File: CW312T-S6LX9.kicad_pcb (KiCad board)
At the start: 2 copper layers, 58.7 x 53.7 mm, 41 parts, among them P1 PCIEx4 EDGE CONNECTOR, U1 XC6SLX9-3TQG144, U2 SST25VF040B-50-4C-SAF-T

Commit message: updated cw312t template
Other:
- outline, holes or cut-outs redrawn

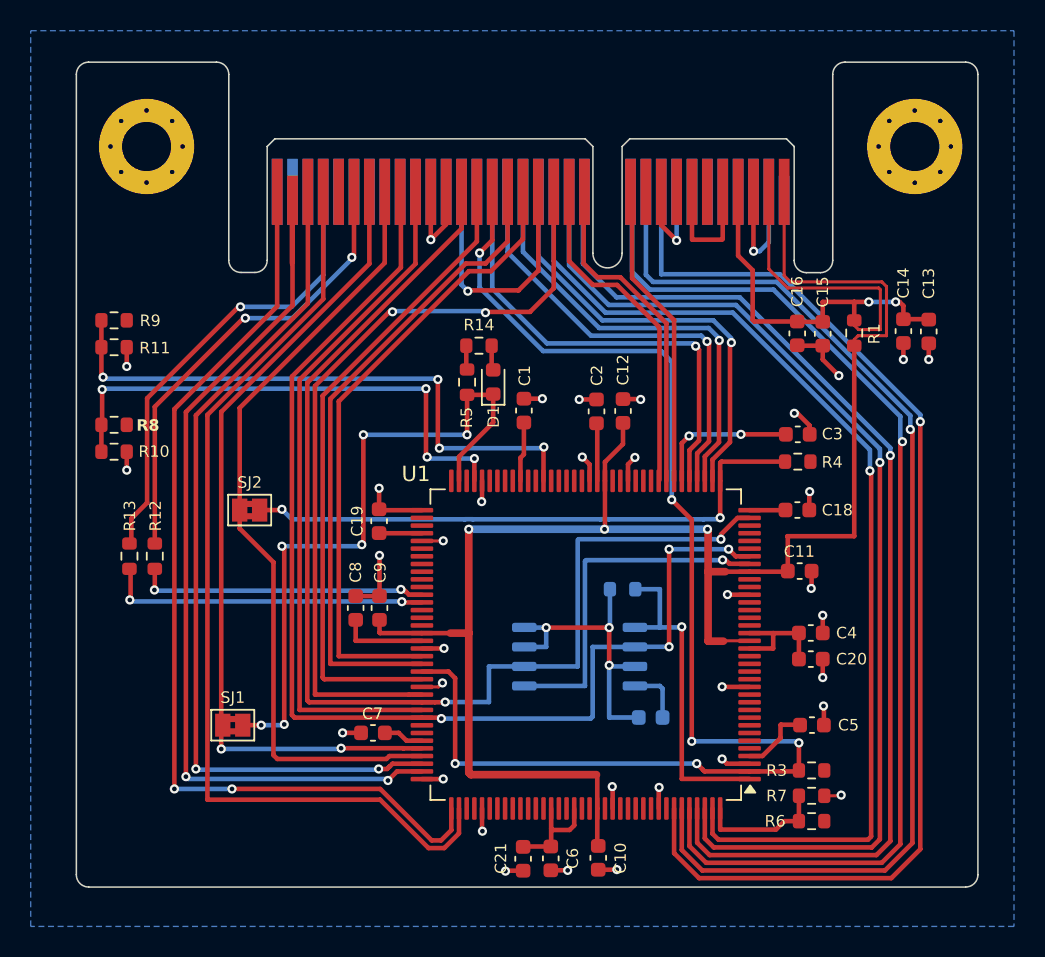
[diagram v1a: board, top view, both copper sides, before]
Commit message: added inner layers for gnd and pwr planes, added silkscreen, updated cw312t template
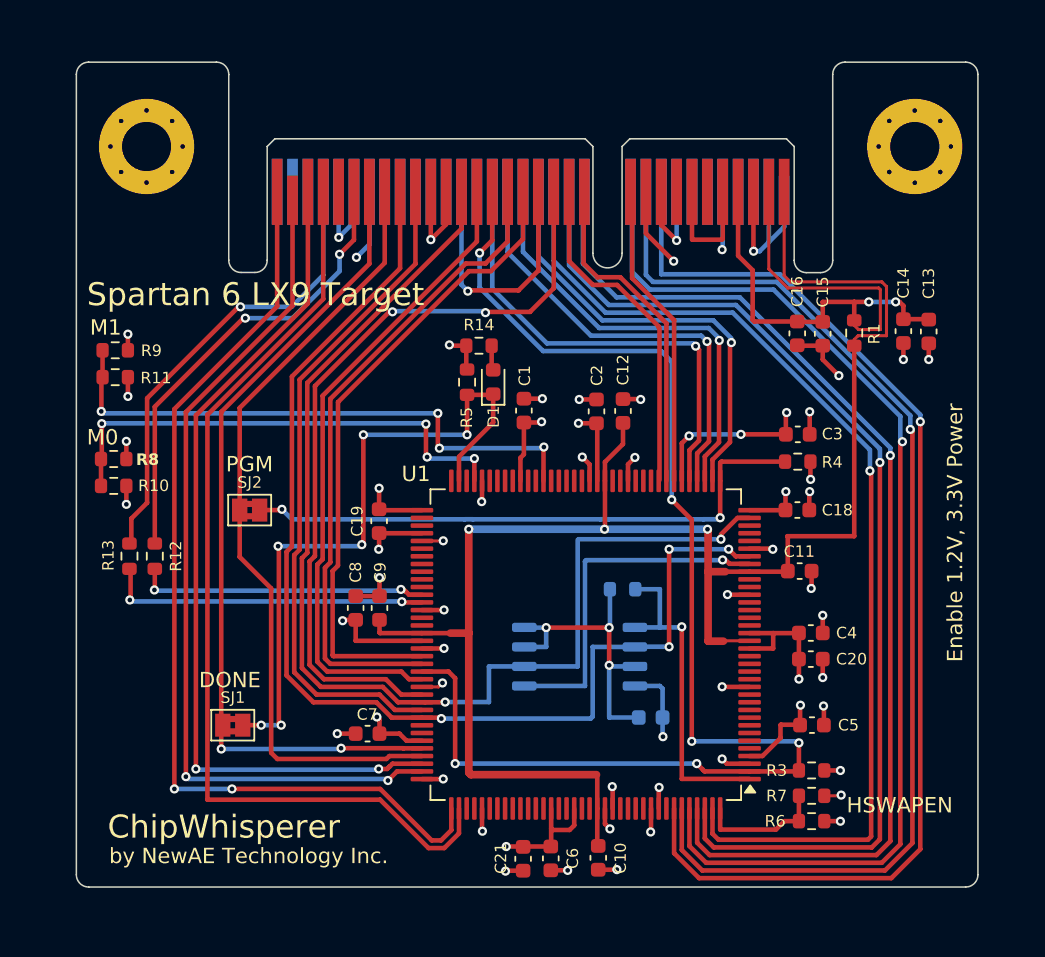
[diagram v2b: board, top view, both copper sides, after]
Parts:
- added PCB1: CE Symbol, Silkscrren_Symbols:CE-Logo_8.5x6mm_SilkScreen, F.Cu at (101.7, 100.5)
- added PCB2: Pb_Free Symbol, Silkscrren_Symbols:Pb_Free_8.0x8.0mm_SilkScreen, F.Cu at (100.6, 91.2)
- added PCB3: UKCA symbol, Silkscrren_Symbols:UKCA-Logo_8x8mm_SilkScreen, F.Cu at (91.7, 91.3)
- added PCB4: WEEE SYMBOL, Silkscrren_Symbols:WEEE-Logo_5.6x8mm_SilkScreen, F.Cu at (91.2, 99.6)
- moved R10 2.23 mm to (89.2, 79.3)
- moved R8 2.23 mm to (89.2, 77.5)
- moved R11 1.95 mm to (89.2, 72.2)
- moved R9 1.95 mm to (89.2, 70.5)
- moved C7 0.35 mm to (105.7, 95.4)
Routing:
- net VCC: track 71.8 -> 110.3 mm, vias 5 -> 28
- net GND: track 96.5 -> 105.4 mm, vias 38 -> 40
- net /XC6SLX9-3TQG144_2/TMS: track 60.2 -> 56.2 mm
- net /XC6SLX9-3TQG144_1/M0: track 34.1 -> 32.0 mm
- net /XC6SLX9-3TQG144_1/M1: track 39.4 -> 37.4 mm
- net /XC6SLX9-3TQG144_1/MOSI: track 78.0 -> 77.0 mm
- net /CW312T-Connector/MISO: track 44.8 -> 43.9 mm
- net /XC6SLX9-3TQG144_1/SCK: track 77.4 -> 76.7 mm
- net /CW312T-Connector/nRST: track 51.6 -> 50.9 mm
- net /CW312T-Connector/GPIO1: track 42.3 -> 42.9 mm
- added copper zone on In2.Cu, net GND
- added copper zone on In1.Cu, net VCC
- removed copper zone on B.Cu, net GND
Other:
- copper layers 2 -> 4
- board text added: "0 1"
- board text added: "1 1"
- board text added: "ChipWhisperer"
- board text added: "DONE"
- board text added: "Enable 1.2V, 3.3V Power"
- board text added: "FPGA Config."
- board text added: "HSWAPEN"
- board text added: "M0"
- board text added: "M1"
- board text added: "Mode"
- board text added: "NewAE Technology Inc. NAE-CW312T-S6LX9 RoHs / Pb-Free"
- board text added: "PGM"
- board text added: "SPI Flash CW-SPI"
- board text added: "SPI Flash Parts"
- board text added: "Spartan 6 LX9 Target"
- board text added: "by NewAE Technology Inc."

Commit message: first draft - ready for review
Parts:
- moved C5 0.91 mm to (134.7, 95.8)
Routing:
- net VCC: track 110.3 -> 109.1 mm
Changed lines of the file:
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@@
 	(footprint "Capacitor_SMD:C_0603_1608Metric"
 		(layer "F.Cu")
-		(at 134.6 94.846318)
+		(at 134.65 95.75)
 		(descr "Capacitor SMD 0603 (1608 Metric), square (rectangular) end terminal, IPC_7351 nominal, (Body size source: IPC-SM-782 page 76, https://www.pcb-3d.com/wordpress/wp-content/uploads/ipc-sm-782a_amendment_1_and_2.pdf), generated with kicad-footprint-generator")
 		(tags "capacitor")
@@
 	)
 	(segment
+		(start 133.875 95.75)
+		(end 133 95.75)
+		(width 0.3)
+		(layer "F.Cu")
+		(net 1)
+	)
+	(segment
 		(start 107.75 95.4)
 		(end 106.45 95.4)
@@
 	)
 	(segment
+		(start 133 95.75)
+		(end 131.891182 96.858818)
+		(width 0.3)
+		(layer "F.Cu")
+		(net 1)
+	)
+	(segment
 		(start 126.6 76.026038)
 		(end 126.125 76.501038)
@@
 	)
 	(segment
+		(start 133.875 94.65)
+		(end 133.875 95.75)
+		(width 0.3)
+		(layer "F.Cu")
+		(net 1)
+	)
+	(segment
 		(start 130.537501 88.858818)
 		(end 132.075 88.858818)
@@
 	)
 	(segment
-		(start 133.825 94.846318)
-		(end 133.825 93.575)
-		(width 0.3)
-		(layer "F.Cu")
-		(net 1)
-	)
-	(segment
 		(start 136.446318 101.096318)
 		(end 136.45 101.1)
@@
 	)
 	(segment
-		(start 133.775 94.771318)
-		(end 133.7 94.846318)
-		(width 0.3)
-		(layer "F.Cu")
-		(net 1)
-	)
-	(segment
 		(start 134.5 78.840997)
 		(end 134.511357 78.852354)
@@
 	)
 	(segment
-		(start 132.55 94.821318)
-		(end 132.55 95.686939)
-		(width 0.3)
-		(layer "F.Cu")
-		(net 1)
-	)
-	(segment
-		(start 133.8 94.821318)
-		(end 132.6 94.821318)
-		(width 0.3)
-		(layer "F.Cu")
-		(net 1)
-	)
-	(segment
 		(start 110.641182 87.358818)
 		(end 110.65 87.35)
@@
 	)
 	(segment
-		(start 131.378121 96.858818)
-		(end 130.537501 96.858818)
-		(width 0.3)
-		(layer "F.Cu")
-		(net 1)
-	)
-	(segment
 		(start 115.625001 78.946318)
 		(end 115.625001 77.45)
@@
 	)
 	(segment
+		(start 131.891182 96.858818)
+		(end 130.537501 96.858818)
+		(width 0.3)
+		(layer "F.Cu")
+		(net 1)
+	)
+	(segment
 		(start 111.049997 70.149997)
 		(end 111 70.1)
@@
 	)
 	(segment
-		(start 133.825 94.846318)
-		(end 133.8 94.821318)
-		(width 0.3)
-		(layer "F.Cu")
-		(net 1)
-	)
-	(segment
 		(start 126.137501 78.933817)
 		(end 126.125 78.946318)
@@
 	)
 	(segment
-		(start 132.55 95.686939)
-		(end 131.378121 96.858818)
-		(width 0.3)
-		(layer "F.Cu")
-		(net 1)
-	)
-	(segment
 		(start 115.625001 77.45)
 		(end 115.85 77.225001)
@@
 	)
 	(segment
-		(start 133.825 93.575)
-		(end 133.85 93.55)
-		(width 0.3)
-		(layer "F.Cu")
-		(net 1)
-	)
-	(segment
 		(start 130.537501 80.858818)
 		(end 132.8625 80.858818)
@@
 	)
 	(segment
-		(start 132.6 94.821318)
-		(end 132.575 94.846318)
-		(width 0.3)
-		(layer "F.Cu")
-		(net 1)
-	)
-	(segment
 		(start 133.675 90.475)
 		(end 133.75 90.55)
@@
 	)
 	(via
-		(at 133.85 93.55)
+		(at 133.875 94.65)
 		(size 0.6)
 		(drill 0.3)
@@
 	)
 	(segment
+		(start 135.4 95.725)
+		(end 135.425 95.75)
+		(width 0.3)
+		(layer "F.Cu")
+		(net 2)
+	)
+	(segment
 		(start 140.550003 71.049997)
 		(end 140.55 71.05)
@@
 	)
 	(segment
-		(start 135.3 70.15)
-		(end 133.665005 70.15)
+		(start 128.255202 97.358818)
+		(end 130.537502 97.358818)
 		(width 0.3)
 		(layer "F.Cu")
@@
 	)
 	(segment
-		(start 135.375 93.625)
-		(end 135.35 93.6)
-		(width 0.2)
+		(start 135.3 70.15)
+		(end 133.665005 70.15)
+		(width 0.3)
 		(layer "F.Cu")
 		(net 2)
@@
 	)
 	(segment
-		(start 135.375 94.846318)
-		(end 135.375 93.625)
-		(width 0.3)
-		(layer "F.Cu")
-		(net 2)
-	)
-	(segment
 		(start 106.45 86.446318)
 		(end 106.45 85.25)
@@
 	)
 	(segment
-		(start 130.537502 97.358818)
-		(end 129.058818 97.358818)
-		(width 0.3)
-		(layer "F.Cu")
-		(net 2)
-	)
-	(segment
 		(start 115.8 104.321318)
 		(end 114.678682 104.321318)
@@
 	)
 	(segment
+		(start 128.105202 97.208818)
+		(end 128.255202 97.358818)
+		(width 0.3)
+		(layer "F.Cu")
+		(net 2)
+	)
+	(segment
 		(start 120.125001 78.946318)
 		(end 120.125001 77.875001)
@@
 	)
 	(segment
+		(start 135.4 94.6)
+		(end 135.4 95.725)
+		(width 0.3)
+		(layer "F.Cu")
+		(net 2)
+	)
+	(segment
 		(start 140.550003 69.975001)
 		(end 140.550003 71.049997)
@@
 	)
 	(segment
-		(start 129.058818 97.358818)
-		(end 128.75 97.05)
-		(width 0.3)
-		(layer "F.Cu")
-		(net 2)
-	)
-	(segment
 		(start 120.125001 77.875001)
 		(end 119.65 77.4)
@@
 	)
 	(via
-		(at 128.75 97.05)
+		(at 128.105202 97.208818)
 		(size 0.6)
 		(drill 0.3)
@@
 	)
 	(via
-		(at 135.35 93.6)
+		(at 135.4 94.6)
 		(size 0.6)
 		(drill 0.3)
@@
 	)
 	(segment
-		(start 133.75 96)
-		(end 133.75 97.796318)
+		(start 126.775 81.482795)
+		(end 125.470846 80.178641)
 		(width 0.3)
 		(layer "F.Cu")
@@
 	)
 	(segment
-		(start 126.775 95.9)
+		(start 126.775 96.65)
 		(end 126.775 81.482795)
 		(width 0.3)
@@
 	)
 	(segment
-		(start 113.79 63.288958)
-		(end 113.79 60.135)
+		(start 133.75 96.85)
+		(end 133.75 97.796318)
 		(width 0.3)
 		(layer "F.Cu")
@@
 	)
 	(segment
-		(start 126.775 81.482795)
-		(end 125.470846 80.178641)
+		(start 113.79 63.288958)
+		(end 113.79 60.135)
 		(width 0.3)
 		(layer "F.Cu")
@@
 	)
 	(via
-		(at 126.775 95.9)
+		(at 126.775 96.65)
 		(size 0.6)
 		(drill 0.3)
@@
 	)
 	(via
-		(at 133.75 96)
+		(at 133.75 96.85)
 		(size 0.6)
 		(drill 0.3)
@@
 	)
 	(segment
-		(start 133.75 96)
-		(end 133.65 95.9)
+		(start 126.866182 96.558818)
+		(end 133.458818 96.558818)
+		(width 0.3)
+		(layer "B.Cu")
+		(net 31)
+	)
+	(segment
+		(start 126.775 96.65)
+		(end 126.866182 96.558818)
 		(width 0.3)
 		(layer "B.Cu")
@@
 	)
 	(segment
-		(start 112.964479 64.114479)
-		(end 112.964479 66.364479)
+		(start 133.458818 96.558818)
+		(end 133.75 96.85)
 		(width 0.3)
 		(layer "B.Cu")
@@
 	)
 	(segment
-		(start 133.65 95.9)
-		(end 126.775 95.9)
+		(start 112.964479 64.114479)
+		(end 112.964479 66.364479)
 		(width 0.3)
 		(layer "B.Cu")
@@
 		(polygon
 			(pts
-				(xy 79.5 49.4) (xy 150.1 49.4) (xy 150.2 49.5) (xy 150.2 108.25) (xy 79.5 108.25) (xy 79.5 49.4)
+				(xy 79.5 49.4) (xy 150.1 49.4) (xy 150.2 49.5) (xy 150.2 108.25) (xy 79.5 108.25)
 			)
 		)
@@
 		(polygon
 			(pts
-				(xy 81.55 50.1) (xy 148.7 50.1) (xy 148.85 50.25) (xy 148.85 107.3) (xy 81.55 107.3) (xy 81.55 107.3)
+				(xy 81.55 50.1) (xy 148.7 50.1) (xy 148.85 50.25) (xy 148.85 107.3) (xy 81.55 107.3)
 			)
 		)

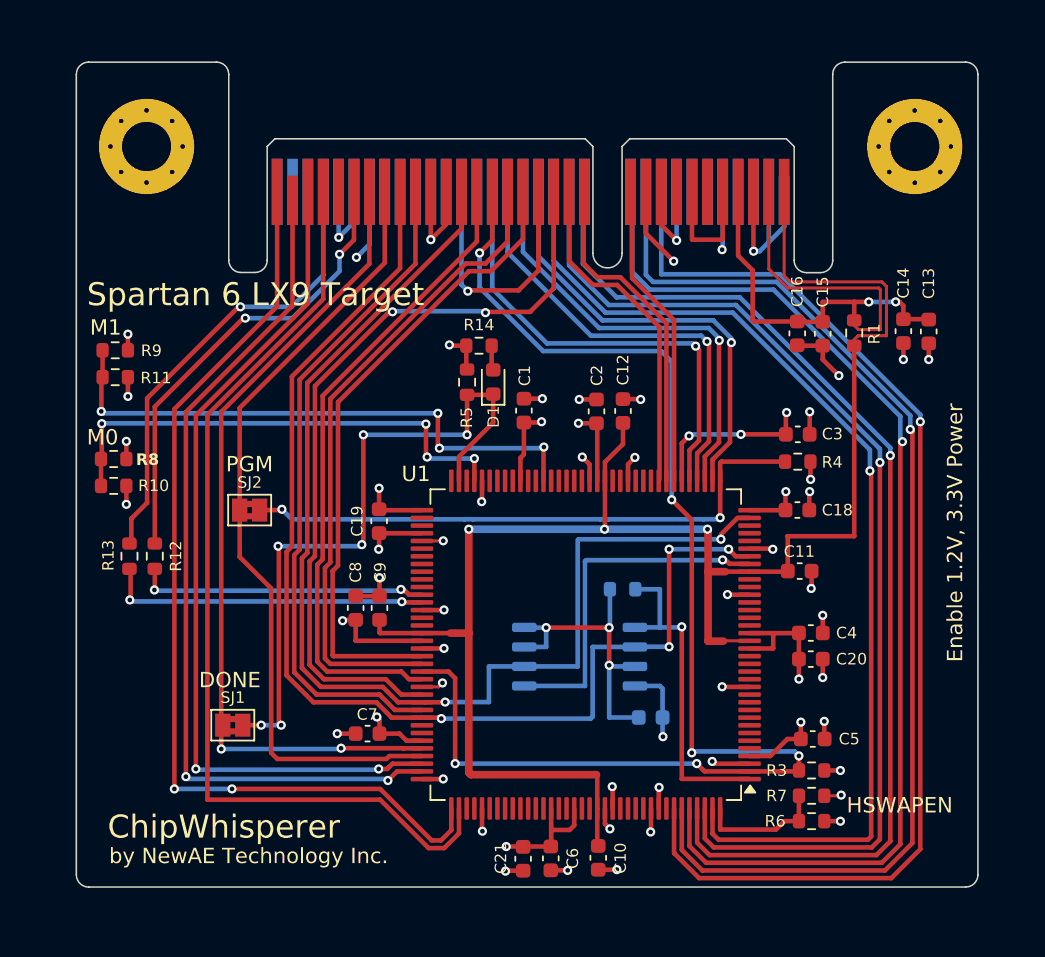
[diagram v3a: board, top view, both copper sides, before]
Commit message: updated schematic and pcb, fixed silkscreen - Ready for review
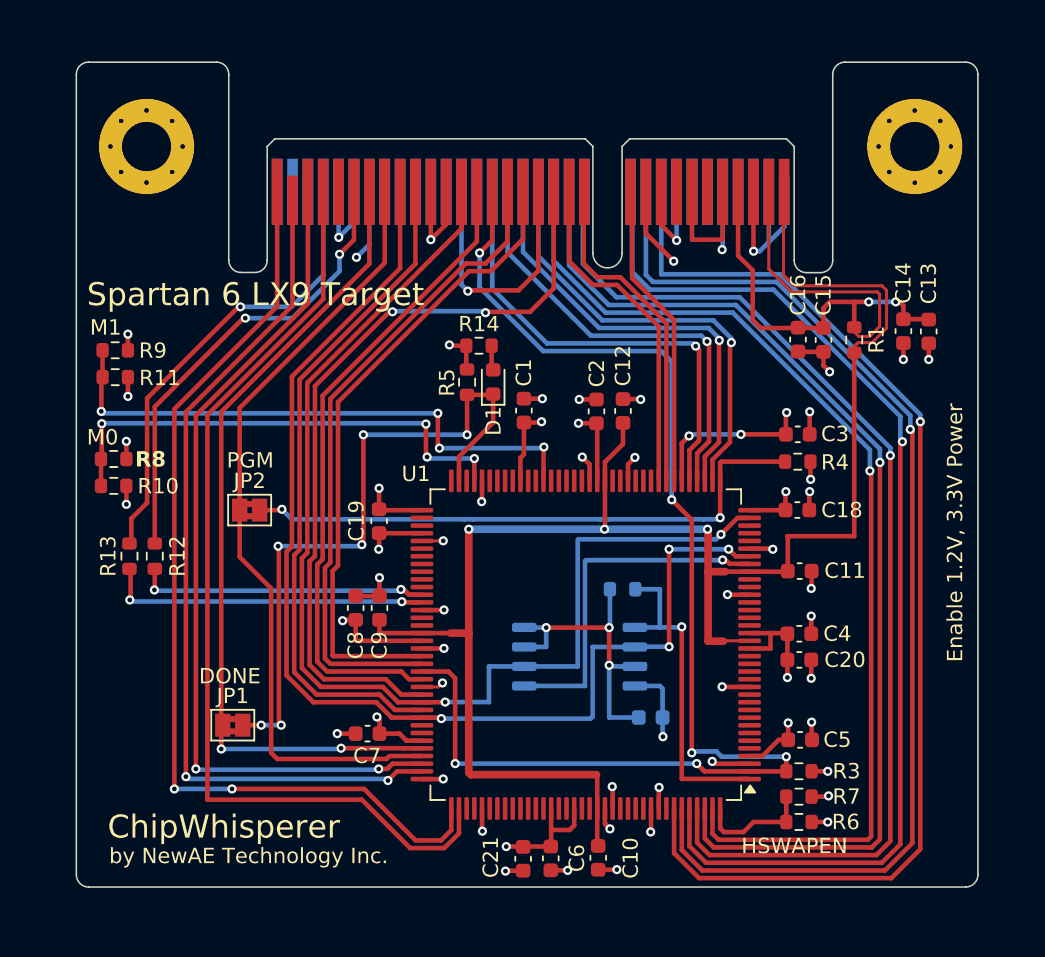
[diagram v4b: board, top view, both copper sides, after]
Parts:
- removed SJ1, SJ2: ~, Jumper:SolderJumper-2_P1.3mm_Bridged2Bar_Pad1.0x1.5mm
- added JP1: ~, Jumper:SolderJumper-2_P1.3mm_Bridged2Bar_Pad1.0x1.5mm, F.Cu at (96.9, 94.8)
- added JP2: ~, Jumper:SolderJumper-2_P1.3mm_Bridged2Bar_Pad1.0x1.5mm, F.Cu at (98.0, 80.8)
- moved C5 0.82 mm to (133.8, 95.8)
- moved R6 0.82 mm to (133.8, 101.2)
- moved R3 0.82 mm to (133.8, 97.8)
- moved R7 0.82 mm to (133.8, 99.5)
- moved C4 0.75 mm to (133.8, 88.9)
- moved C20 0.75 mm to (133.8, 90.6)
- moved R1 0.45 mm to (137.3, 69.8)
- moved C15 0.40 mm to (135.3, 69.8)
- moved C16 0.40 mm to (133.7, 69.7)
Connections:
- net /XC6SLX9-3TQG144_1/MOSI renamed MOSI
- net /XC6SLX9-3TQG144_1/SCK renamed SCK
- net /XC6SLX9-3TQG144_2/TCK renamed /CW312T-Connector/TCK
- net /XC6SLX9-3TQG144_2/TDI renamed /CW312T-Connector/TDI
- net /XC6SLX9-3TQG144_2/TDO renamed /CW312T-Connector/TDO
- net /XC6SLX9-3TQG144_2/TMS renamed /CW312T-Connector/TMS
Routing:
- net VCC: track 109.1 -> 107.2 mm
- net /CW312T-Connector/GPIO3: track 85.7 -> 84.2 mm
- net GND: track 105.8 -> 104.9 mm
- net Net-(U1A-IO_L1P_HSWAPEN_0): track 8.59 -> 7.84 mm
- net /CW312T-Connector/SHUNTL: track 110.9 -> 110.3 mm

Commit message: updated schematic and pcb after library re-organization
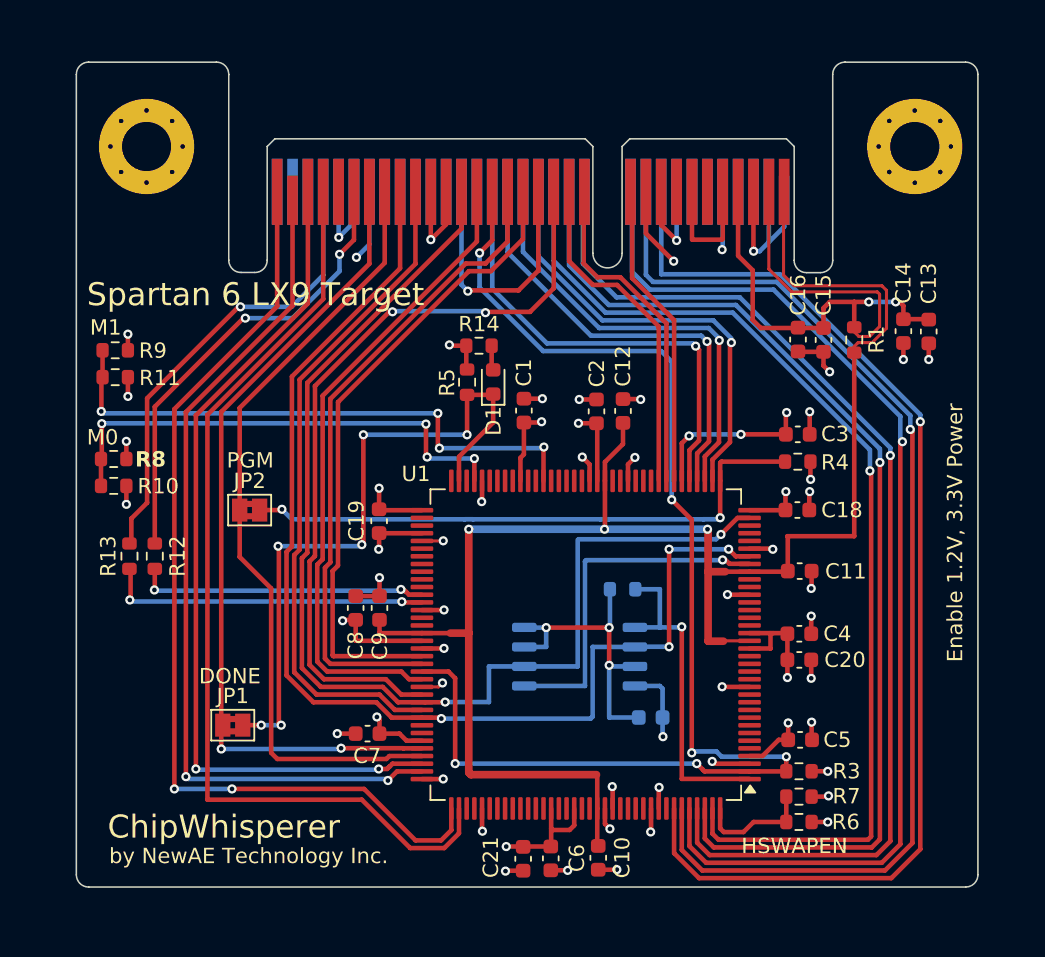
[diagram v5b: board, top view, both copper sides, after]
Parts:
- R10, R11: value RES_2k2_0603 -> RES_1k_0603
- R7: value DNM_0603 -> RES_1k_0603
- turned C10 to 90 degrees
- turned C11 to 180 degrees
- turned C12 to -90 degrees
- turned C9 to -90 degrees
- turned R7 to 180 degrees
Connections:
- C10 pad 1: /CW312T-Connector/SHUNTL -> GND
- C10 pad 2: GND -> /CW312T-Connector/SHUNTL
- C11 pad 1: /CW312T-Connector/SHUNTL -> GND
- C11 pad 2: GND -> /CW312T-Connector/SHUNTL
- C12 pad 1: /CW312T-Connector/SHUNTL -> GND
- C12 pad 2: GND -> /CW312T-Connector/SHUNTL
- C9 pad 1: /CW312T-Connector/SHUNTL -> GND
- C9 pad 2: GND -> /CW312T-Connector/SHUNTL
- R7 pad 1: Net-(U1A-IO_L1P_HSWAPEN_0) -> GND
- R7 pad 2: GND -> Net-(U1A-IO_L1P_HSWAPEN_0)
